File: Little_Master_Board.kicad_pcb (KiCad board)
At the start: 2 copper layers, 46.3 x 21.7 mm, 14 parts, among them J1 02x07 Header, J2 01x02 Header, J3 2.5mm Audio Jack, U1 SP3222EUEY-L_TR

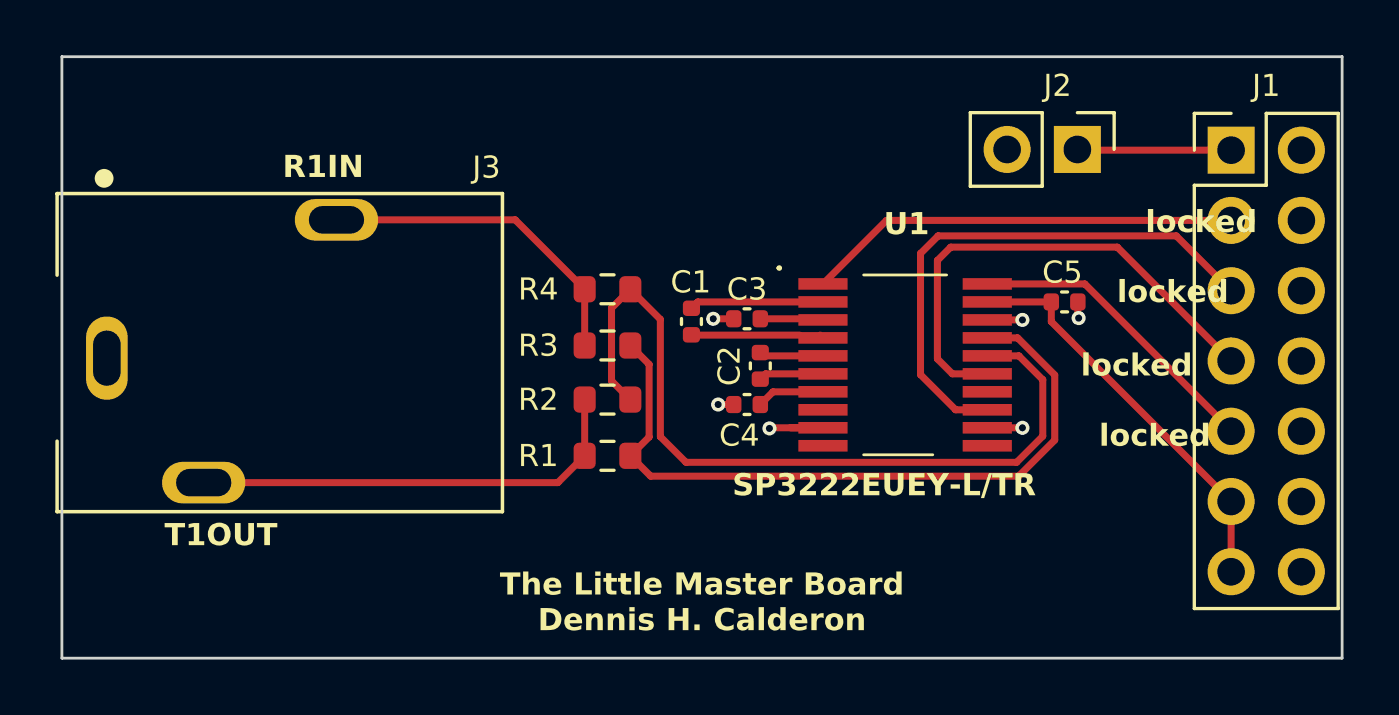
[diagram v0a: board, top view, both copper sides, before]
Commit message: Fab files for Rev B updated. Removed SHDN on pin. Connected to VCC for HIGH. Added 2 pin header to pin 2 on 2x7 header. EN routed to pin 5 on 2x7 header.
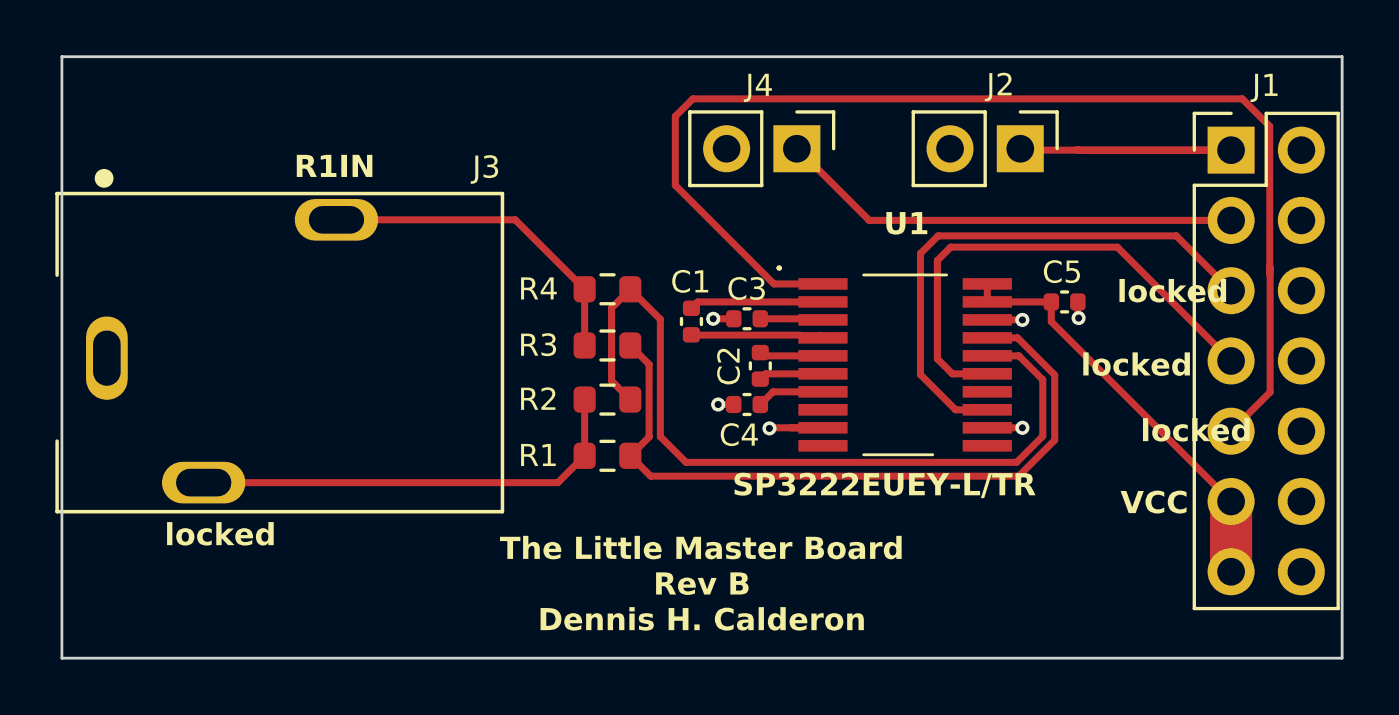
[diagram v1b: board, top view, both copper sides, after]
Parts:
- added J4: 01x02 Header, Connector_PinHeader_2.54mm:PinHeader_1x02_P2.54mm_Vertical, F.Cu at (138.3, 61.5)
- moved J2 2.06 mm to (146.4, 61.5)
- moved G*** 1.30 mm to (141.3, 67.9)
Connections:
- J1 pad 2: /~{EN} -> Net-(J1-Pin_2)
- J1 pad 5: /~{SHDN} -> /~{EN}
- U1 pad 20: /~{SHDN} -> VCC
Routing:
- net /~{EN}: track 15.7 -> 43.3 mm
- net Net-(J1-Pin_2): track 0.00 -> 16.8 mm
- net /~{SHDN}: track 11.0 -> 0.00 mm
- net Net-(J1-Pin_1): track 5.57 -> 13.2 mm
- net VCC: track 14.8 -> 15.4 mm
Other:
- board text added: "The Little Master Board Rev B Dennis H. Calderon"
- board text added: "VCC"
- board text removed: "The Little Master Board Dennis H. Calderon"
